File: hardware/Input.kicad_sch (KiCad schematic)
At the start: 40 parts, among them J1 AudioJack3, J2 Conn_Coaxial, J3 Conn_Coaxial, J4 Conn_Coaxial, J5 Conn_Coaxial, J6 Barrel_Jack_Switch, J7 USB_C_Receptacle_PowerOnly_6P, U6 74LVCH2T45DC, U7 74LVCH2T45DC, U8 74LVCH2T45DC

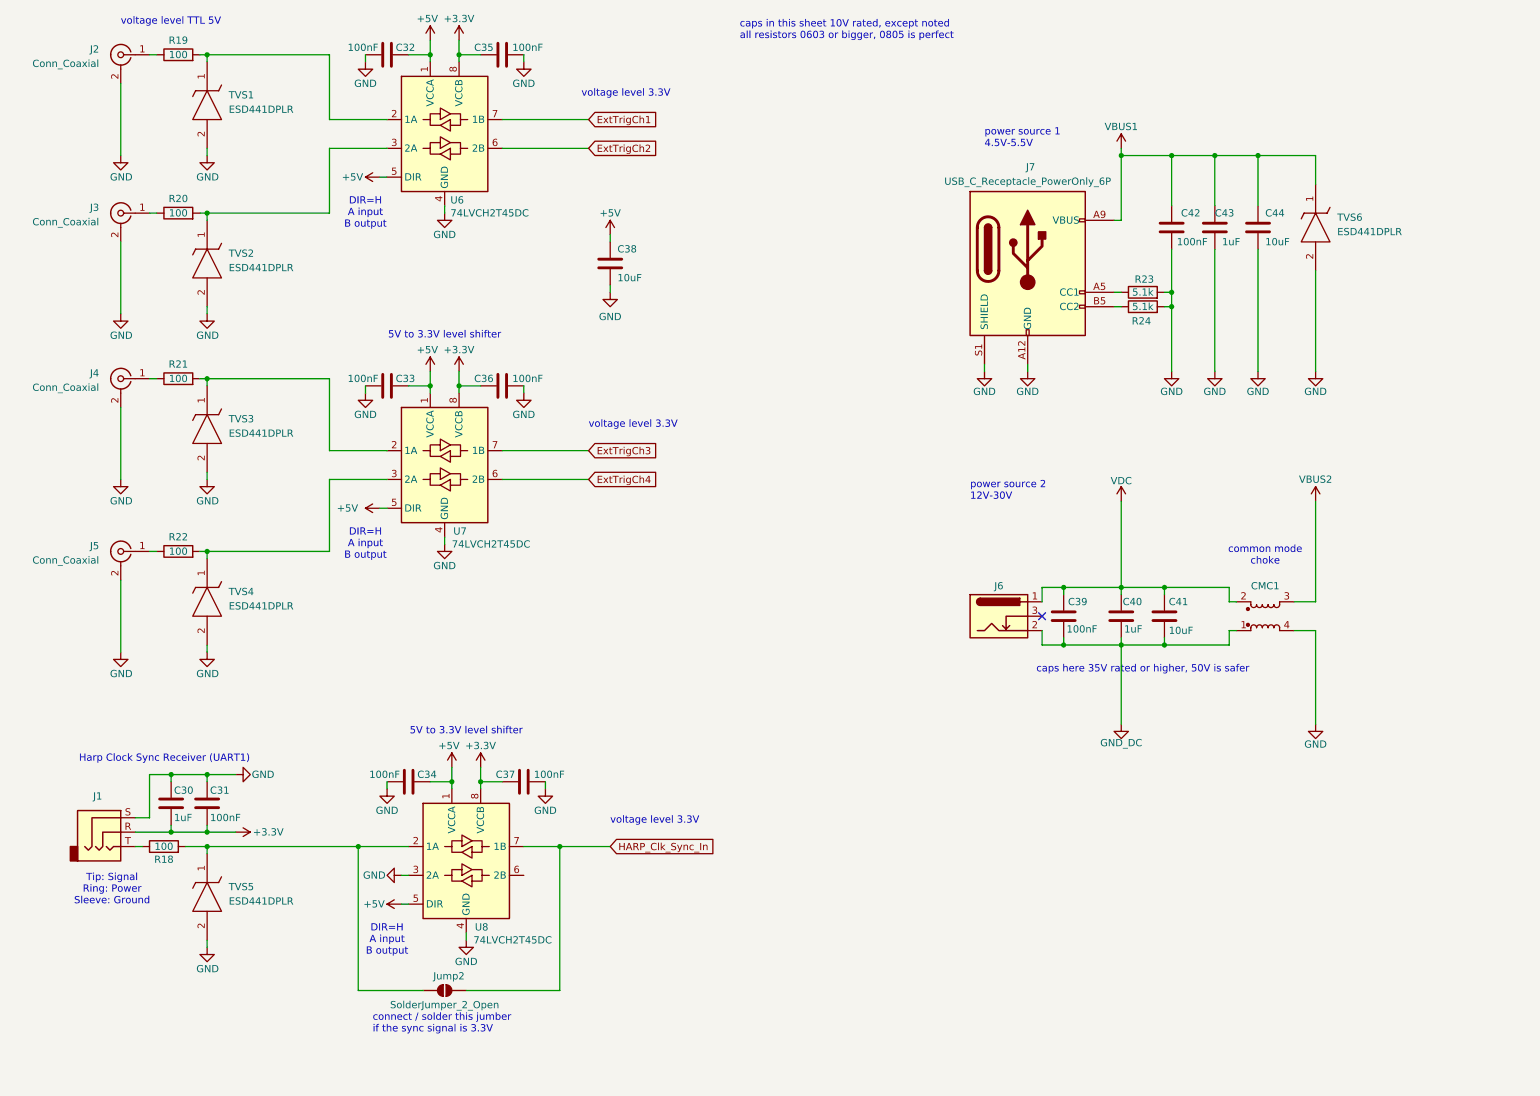
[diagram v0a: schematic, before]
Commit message: Added caps voltage rating + block diagram
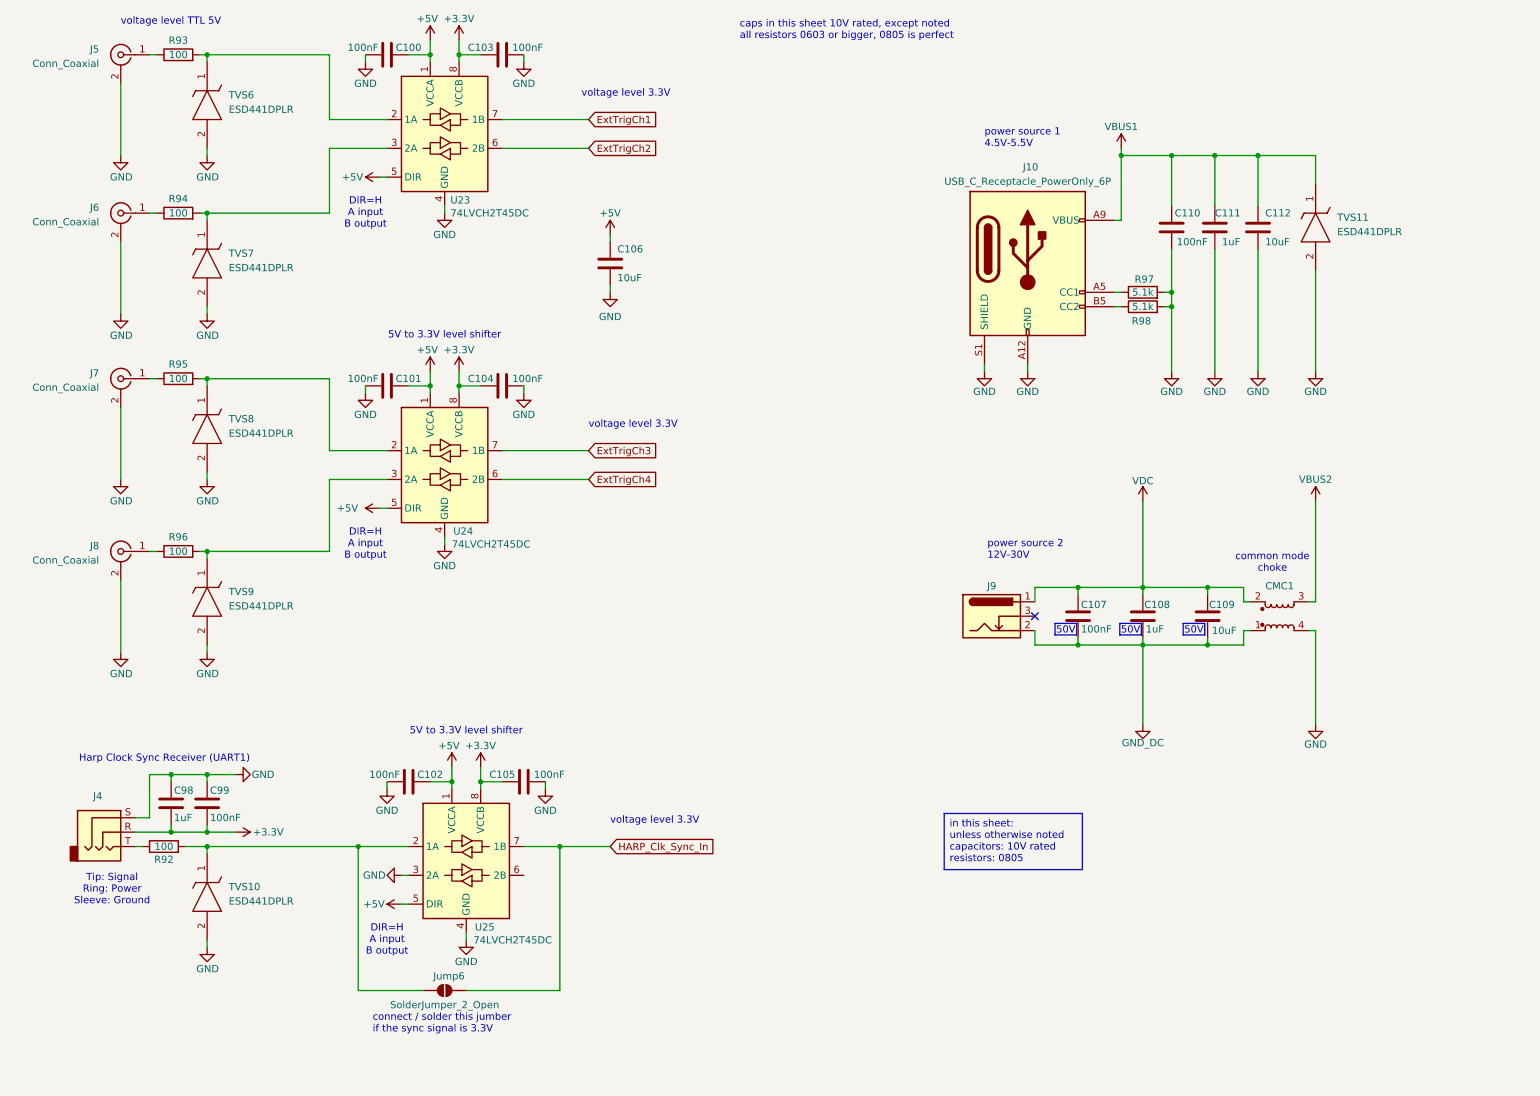
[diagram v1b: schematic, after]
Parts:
- renumbered C32 to C100, C33 to C101, C34 to C102, C35 to C103, C36 to C104, C37 to C105, C38 to C106, C39 to C107, C40 to C108, C41 to C109, C42 to C110, C43 to C111, C44 to C112, C30 to C98, C31 to C99, J7 to J10, J1 to J4, J2 to J5, J3 to J6, J4 to J7, J5 to J8, J6 to J9, Jump2 to Jump6, R18 to R92, R19 to R93, R20 to R94, R21 to R95, R22 to R96, R23 to R97, R24 to R98, TVS5 to TVS10, TVS6 to TVS11, TVS1 to TVS6, TVS2 to TVS7, TVS3 to TVS8, TVS4 to TVS9, U6 to U23, U7 to U24, U8 to U25
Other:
- note removed: "caps here 35V rated or higher, 50V is safer"
- title: Multi Channel HARP DAC -> harp device quad dac
- moved on the sheet: C107, C108, C109, CMC1, J9

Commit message: The footprint assigning and reviewing have started.
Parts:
- C100, C101, C102, C103, C104, C105, C106, C107, C108, C109, C110, C111, C112, C98, C99: symbol Device:C -> harp.device.quad.dac:C
- CMC1: symbol Device:L_Coupled_1423 -> harp.device.quad.dac:L_Coupled_1423
- J10: symbol Connector:USB_C_Receptacle_PowerOnly_6P -> harp.device.quad.dac:USB_C_Receptacle_PowerOnly_6P
- J4: symbol Connector:AudioJack3 -> harp.device.quad.dac:AudioJack3
- J5, J6, J7, J8: symbol Connector:Conn_Coaxial -> harp.device.quad.dac:Conn_Coaxial
- J9: symbol Connector:Barrel_Jack_Switch -> harp.device.quad.dac:Barrel_Jack_Switch
- Jump6: symbol Jumper:SolderJumper_2_Open -> harp.device.quad.dac:SolderJumper_2_Open
- R92, R93, R94, R95, R96, R97, R98: symbol Device:R -> harp.device.quad.dac:R
- TVS10, TVS11, TVS6, TVS7, TVS8, TVS9: symbol ESD441DPLR:ESD441DPLR -> harp.device.quad.dac:ESD441DPLR
- U23, U24, U25: symbol Logic_LevelTranslator:74LVCH2T45DC -> harp.device.quad.dac:74LVCH2T45DC
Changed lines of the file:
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@@
 	)
 	(symbol
-		(lib_id "Logic_LevelTranslator:74LVCH2T45DC")
+		(lib_id "harp.device.quad.dac:74LVCH2T45DC")
 		(at 88.9 35.56 0)
 		(unit 1)
@@
 	)
 	(symbol
-		(lib_id "Device:C")
+		(lib_id "harp.device.quad.dac:C")
 		(at 40.64 153.67 0)
 		(unit 1)
@@
 	)
 	(symbol
-		(lib_id "Device:C")
+		(lib_id "harp.device.quad.dac:C")
 		(at 217.17 52.07 180)
 		(unit 1)
@@
 	)
 	(symbol
-		(lib_id "ESD441DPLR:ESD441DPLR")
+		(lib_id "harp.device.quad.dac:ESD441DPLR")
 		(at 46.99 80.01 270)
 		(unit 1)
@@
 	)
 	(symbol
-		(lib_id "Connector:Barrel_Jack_Switch")
+		(lib_id "harp.device.quad.dac:Barrel_Jack_Switch")
 		(at 185.42 120.65 0)
 		(unit 1)
@@
 	)
 	(symbol
-		(lib_id "Device:R")
+		(lib_id "harp.device.quad.dac:R")
 		(at 212.09 66.04 90)
 		(unit 1)
@@
 	)
 	(symbol
-		(lib_id "Device:C")
+		(lib_id "harp.device.quad.dac:C")
 		(at 232.41 52.07 0)
 		(unit 1)
@@
 	)
 	(symbol
-		(lib_id "Device:C")
+		(lib_id "harp.device.quad.dac:C")
 		(at 200.66 120.65 180)
 		(unit 1)
@@
 	)
 	(symbol
-		(lib_id "Device:C")
+		(lib_id "harp.device.quad.dac:C")
 		(at 223.52 120.65 0)
 		(unit 1)
@@
 	)
 	(symbol
-		(lib_id "Device:C")
+		(lib_id "harp.device.quad.dac:C")
 		(at 102.87 149.86 270)
 		(unit 1)
@@
 	)
 	(symbol
-		(lib_id "Connector:Conn_Coaxial")
+		(lib_id "harp.device.quad.dac:Conn_Coaxial")
 		(at 31.75 49.53 0)
 		(mirror y)
@@
 	)
 	(symbol
-		(lib_id "Logic_LevelTranslator:74LVCH2T45DC")
+		(lib_id "harp.device.quad.dac:74LVCH2T45DC")
 		(at 92.71 163.83 0)
 		(unit 1)
@@
 	)
 	(symbol
-		(lib_id "Device:R")
+		(lib_id "harp.device.quad.dac:R")
 		(at 41.91 109.22 90)
 		(unit 1)
@@
 	)
 	(symbol
-		(lib_id "Device:R")
+		(lib_id "harp.device.quad.dac:R")
 		(at 41.91 49.53 90)
 		(unit 1)
@@
 	)
 	(symbol
-		(lib_id "Connector:Conn_Coaxial")
+		(lib_id "harp.device.quad.dac:Conn_Coaxial")
 		(at 31.75 109.22 0)
 		(mirror y)
@@
 	)
 	(symbol
-		(lib_id "Connector:Conn_Coaxial")
+		(lib_id "harp.device.quad.dac:Conn_Coaxial")
 		(at 31.75 21.59 0)
 		(mirror y)
@@
 	)
 	(symbol
-		(lib_id "ESD441DPLR:ESD441DPLR")
+		(lib_id "harp.device.quad.dac:ESD441DPLR")
 		(at 46.99 22.86 270)
 		(unit 1)
@@
 	)
 	(symbol
-		(lib_id "Device:C")
+		(lib_id "harp.device.quad.dac:C")
 		(at 78.74 21.59 270)
 		(unit 1)
@@
 	)
 	(symbol
-		(lib_id "Device:L_Coupled_1423")
+		(lib_id "harp.device.quad.dac:L_Coupled_1423")
 		(at 236.22 120.65 0)
 		(mirror x)
@@
 	)
 	(symbol
-		(lib_id "Device:R")
+		(lib_id "harp.device.quad.dac:R")
 		(at 39.37 161.29 90)
 		(unit 1)
@@
 	)
 	(symbol
-		(lib_id "ESD441DPLR:ESD441DPLR")
+		(lib_id "harp.device.quad.dac:ESD441DPLR")
 		(at 242.57 44.45 270)
 		(unit 1)
@@
 	)
 	(symbol
-		(lib_id "Device:C")
+		(lib_id "harp.device.quad.dac:C")
 		(at 118.11 58.42 0)
 		(unit 1)
@@
 	)
 	(symbol
-		(lib_id "Device:C")
+		(lib_id "harp.device.quad.dac:C")
 		(at 99.06 21.59 270)
 		(unit 1)
@@
 	)
 	(symbol
-		(lib_id "ESD441DPLR:ESD441DPLR")
+		(lib_id "harp.device.quad.dac:ESD441DPLR")
 		(at 46.99 162.56 270)
 		(unit 1)
@@
 	)
 	(symbol
-		(lib_id "Logic_LevelTranslator:74LVCH2T45DC")
+		(lib_id "harp.device.quad.dac:74LVCH2T45DC")
 		(at 88.9 93.98 0)
 		(unit 1)
@@
 	)
 	(symbol
-		(lib_id "Connector:USB_C_Receptacle_PowerOnly_6P")
+		(lib_id "harp.device.quad.dac:USB_C_Receptacle_PowerOnly_6P")
 		(at 191.77 58.42 0)
 		(unit 1)
@@
 	)
 	(symbol
-		(lib_id "Device:C")
+		(lib_id "harp.device.quad.dac:C")
 		(at 99.06 80.01 270)
 		(unit 1)
@@
 	)
 	(symbol
-		(lib_id "Device:R")
+		(lib_id "harp.device.quad.dac:R")
 		(at 41.91 21.59 90)
 		(unit 1)
@@
 	)
 	(symbol
-		(lib_id "Jumper:SolderJumper_2_Open")
+		(lib_id "harp.device.quad.dac:SolderJumper_2_Open")
 		(at 88.9 186.69 0)
 		(unit 1)
@@
 	)
 	(symbol
-		(lib_id "Connector:AudioJack3")
+		(lib_id "harp.device.quad.dac:AudioJack3")
 		(at 29.21 158.75 0)
 		(unit 1)
@@
 	)
 	(symbol
-		(lib_id "Device:R")
+		(lib_id "harp.device.quad.dac:R")
 		(at 212.09 63.5 90)
 		(unit 1)
@@
 	)
 	(symbol
-		(lib_id "Device:R")
+		(lib_id "harp.device.quad.dac:R")
 		(at 41.91 78.74 90)
 		(unit 1)
@@
 	)
 	(symbol
-		(lib_id "Device:C")
+		(lib_id "harp.device.quad.dac:C")
 		(at 224.79 52.07 0)
 		(unit 1)
@@
 	)
 	(symbol
-		(lib_id "Device:C")
+		(lib_id "harp.device.quad.dac:C")
 		(at 78.74 80.01 270)
 		(unit 1)
@@
 	)
 	(symbol
-		(lib_id "Connector:Conn_Coaxial")
+		(lib_id "harp.device.quad.dac:Conn_Coaxial")
 		(at 31.75 78.74 0)
 		(mirror y)
@@
 	)
 	(symbol
-		(lib_id "Device:C")
+		(lib_id "harp.device.quad.dac:C")
 		(at 46.99 153.67 180)
 		(unit 1)
@@
 	)
 	(symbol
-		(lib_id "Device:C")
+		(lib_id "harp.device.quad.dac:C")
 		(at 212.09 120.65 0)
 		(unit 1)
@@
 	)
 	(symbol
-		(lib_id "ESD441DPLR:ESD441DPLR")
+		(lib_id "harp.device.quad.dac:ESD441DPLR")
 		(at 46.99 50.8 270)
 		(unit 1)
@@
 	)
 	(symbol
-		(lib_id "Device:C")
+		(lib_id "harp.device.quad.dac:C")
 		(at 82.55 149.86 270)
 		(unit 1)
@@
 	)
 	(symbol
-		(lib_id "ESD441DPLR:ESD441DPLR")
+		(lib_id "harp.device.quad.dac:ESD441DPLR")
 		(at 46.99 110.49 270)
 		(unit 1)

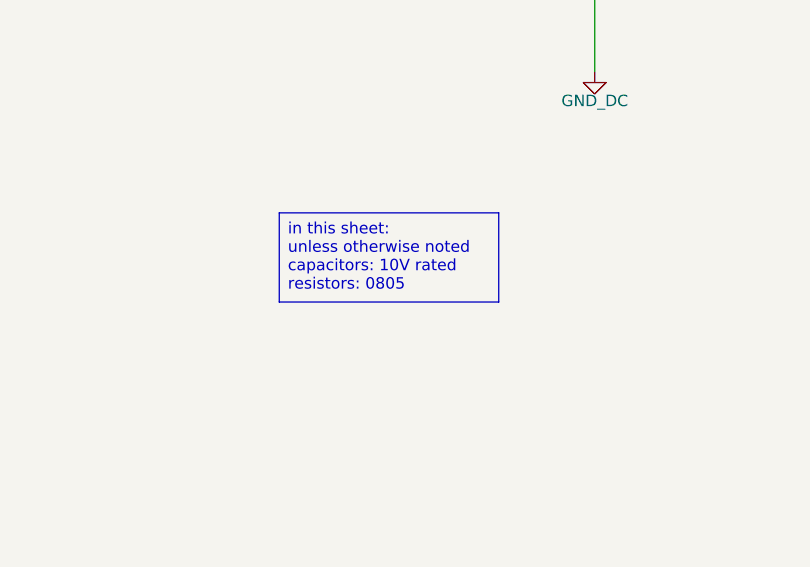
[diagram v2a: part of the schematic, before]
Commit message: Modified notes about caps and resistors
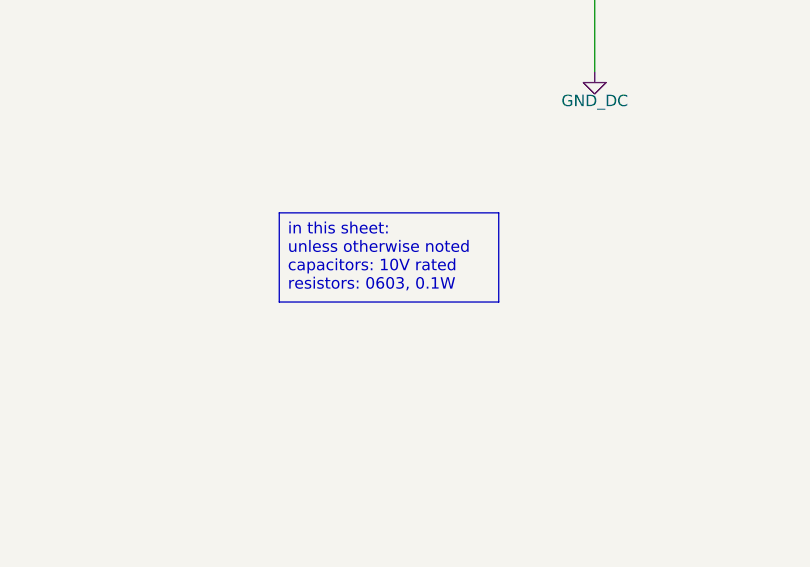
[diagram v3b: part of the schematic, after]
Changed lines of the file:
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@@
 		)
 	)
-	(text_box "in this sheet:\nunless otherwise noted\ncapacitors: 10V rated \nresistors: 0805"
+	(text_box "in this sheet:\nunless otherwise noted\ncapacitors: 10V rated \nresistors: 0603, 0.1W"
 		(exclude_from_sim no)
 		(at 177.038 155.448 0)

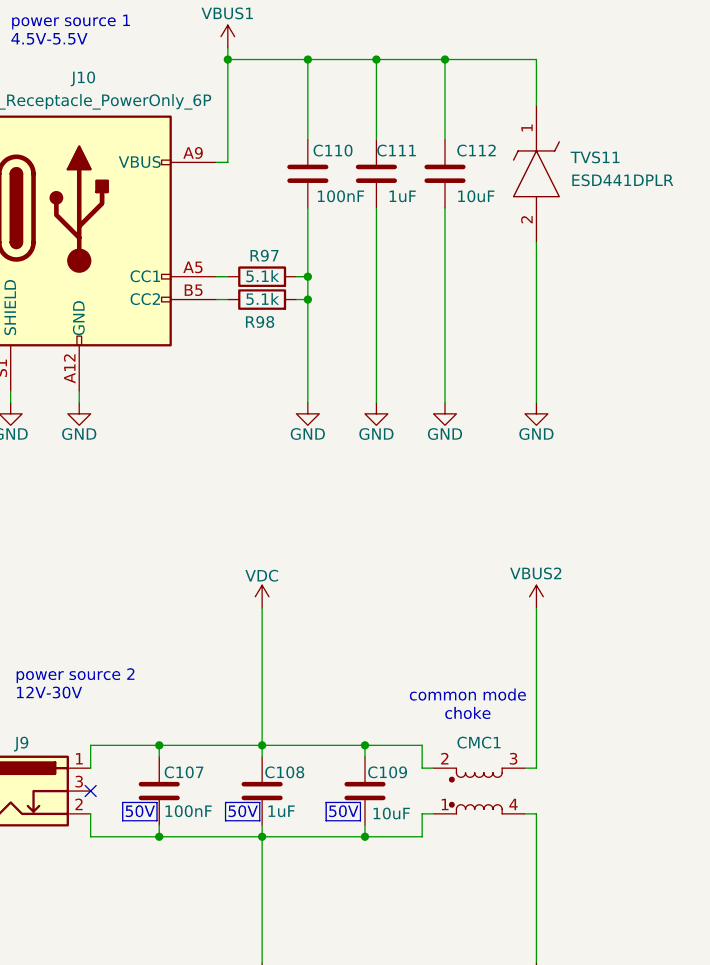
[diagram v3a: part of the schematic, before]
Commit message: Updating some footprints
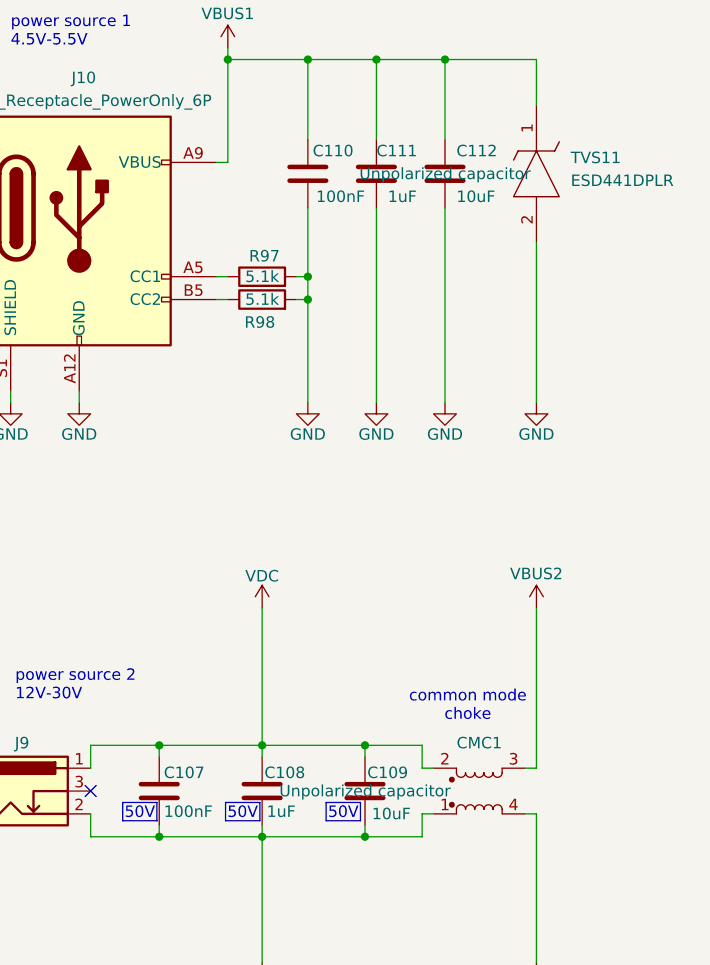
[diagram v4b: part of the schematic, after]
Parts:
- C100, C101, C102, C103, C104, C105, C107, C108, C110, C111, C98, C99: footprint Capacitor_SMD:C_0402_1005Metric -> Capacitor_SMD:C_0603_1608Metric; symbol harp.device.quad.dac:C -> harp.device.quad.dac:C_0603
- C106, C109, C112: footprint Capacitor_SMD:C_0805_2012Metric -> Capacitor_SMD:C_0603_1608Metric; symbol harp.device.quad.dac:C -> harp.device.quad.dac:C_0603
- Jump6: footprint (none) -> harp.device.quad.dac.kicad:R_0603_1608Metric_Pad0.98x0.95mm_HandSolder
- R92, R93, R94, R95, R96, R97, R98: footprint Resistor_SMD:R_0402_1005Metric -> Resistor_SMD:R_0603_1608Metric; symbol harp.device.quad.dac:R -> harp.device.quad.dac:R_0603

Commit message: The layout design has begun.
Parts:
- removed J10: USB_C_Receptacle_PowerOnly_6P, symbol harp.device.quad.dac:USB_C_Receptacle_PowerOnly_6P
- added J24: Conn_01x02, Connector_PinHeader_2.54mm:PinHeader_1x02_P2.54mm_Vertical, symbol harp.device.quad.dac:Conn_01x02
- added J27: USB_C_Receptacle_USB2.0, harp.device.quad.dac.kicad:USB_C_Receptacle_JAE_DX07S016JA1R1500, symbol harp.device.quad.dac:USB_C_Receptacle_USB2.0
- CMC1: footprint kicad_component_library:L_CommonModeChoke_TDKCorporation_1210 -> harp.device.quad.dac.kicad:L_CommonModeChoke_TDKCorporation_1210
- J4: footprint Connector_Audio:Jack_3.5mm_CUI_SJ-3524-SMT_Horizontal -> harp.device.quad.dac.kicad:Jack_3.5mm_CUI_SJ-3524-SMT_Horizontal
- J5, J6, J7, J8: footprint (none) -> harp.device.quad.dac.kicad:SMA_TE_Connectivity_CONSMA002-SMD-G-T_Horizontal
- U23, U24, U25: footprint Package_SO:VSSOP-8_2.3x2mm_P0.5mm -> harp.device.quad.dac.kicad:VSSOP-8_2.3x2mm_P0.5mm
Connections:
- net GND: now also J27.A1 (GND), J27.A12 (GND), J27.B1 (GND), J27.B12 (GND), J27.S1 (SHIELD)
- net HARP_Clk_Sync_In: now also J24.1 (Pin_1)
- net VBUS1: now also J27.A4 (VBUS), J27.A9 (VBUS), J27.B4 (VBUS), J27.B9 (VBUS)
- net at R98.1: now also J27.B5 (CC2)
- net at Jump6.1 (A), R92.2, TVS10.1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: now also J24.2 (Pin_2)
- net at R97.1: now also J27.A5 (CC1)
- no-connect marks 1 -> 8
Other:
- moved on the sheet: C107, C108, C109, C110, C111, C112, CMC1, J9, R97, R98, TVS11
